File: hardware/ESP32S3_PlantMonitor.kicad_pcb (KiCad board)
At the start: 4 copper layers, 62.5 x 44.5 mm, 69 parts, among them J1 USB_C_Receptacle_USB2.0_16P, J2 Conn_01x03, J3 Conn_01x02, Q1 AO3401A, Q2 AO3401A, Q3 AO3401A, SW1 SW_Push, SW2 SW_Push, U1 USBLC6-2SC6, U2 AP2112K-3.3, U3 ESP32-S3-WROOM-1, U4 BME280, U5 VEML7700-TT, U6 MCP73831-2-OT

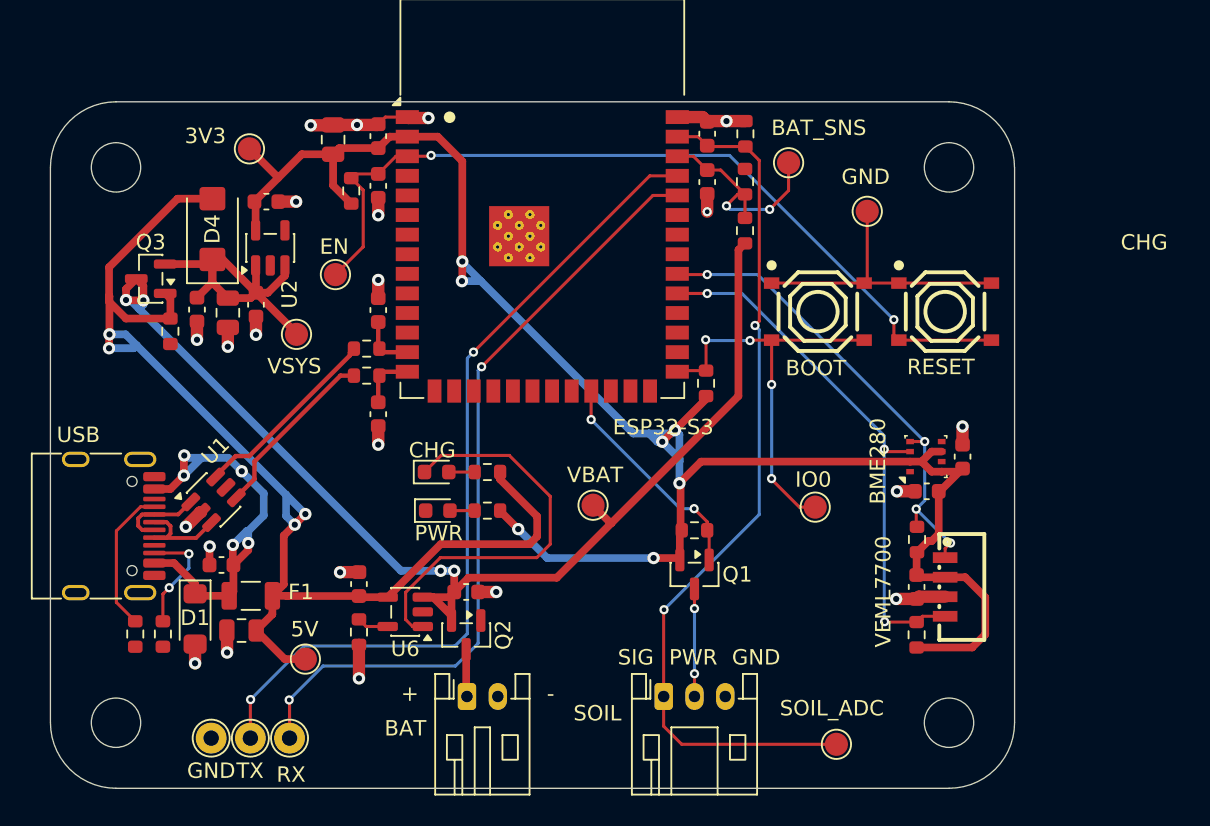
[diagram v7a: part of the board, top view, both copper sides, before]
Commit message: Add stitching and remaining vias
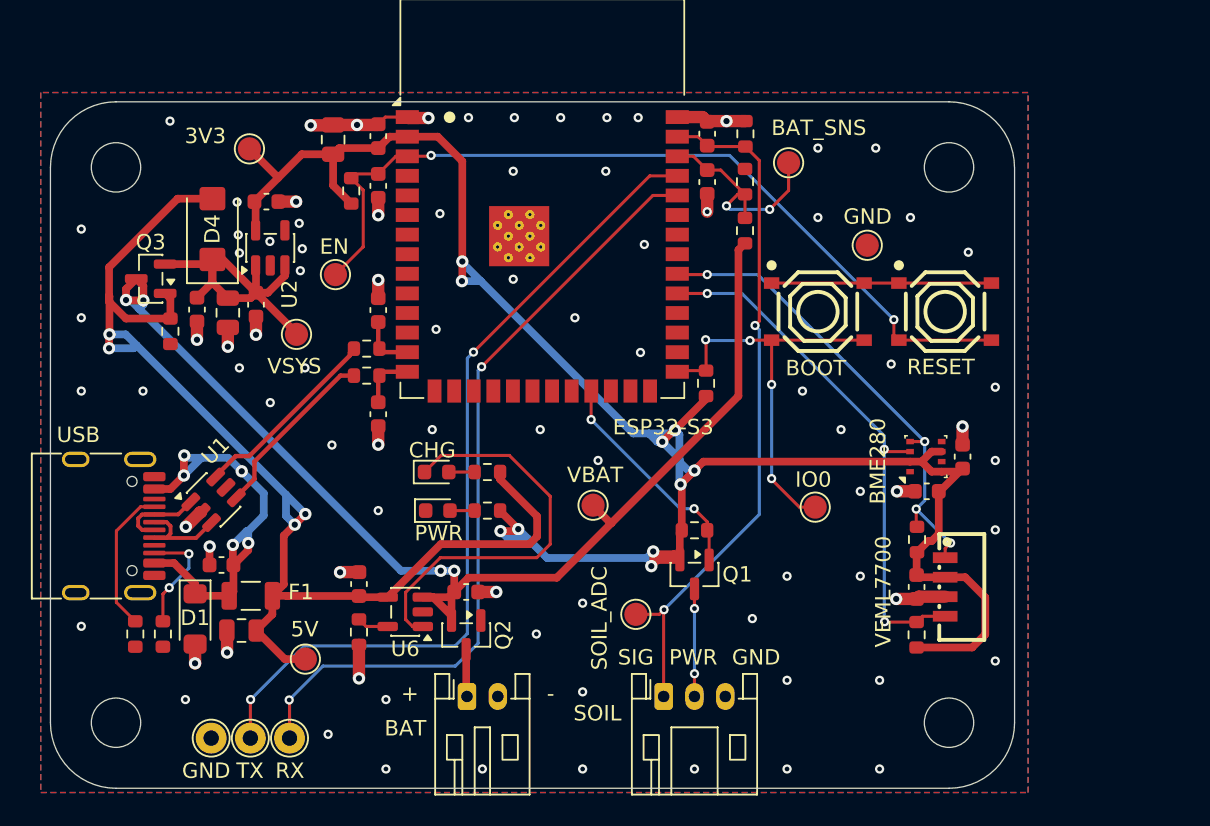
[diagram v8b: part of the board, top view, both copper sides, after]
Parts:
- moved TP6 15.5 mm to (72.0, 83.2)
- moved TP7 2.20 mm to (87.0, 59.3)
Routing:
- net ADC_SOIL: track 57.1 -> 45.4 mm
- net +3V3: track 121.8 -> 131.3 mm, vias 7 -> 10
- net GND: track 56.4 -> 51.9 mm, vias 22 -> 86
- added copper zone on B.Cu, net GND
- added copper zone on F.Cu, net GND
